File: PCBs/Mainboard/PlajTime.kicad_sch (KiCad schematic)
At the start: 7 parts, among them IC5 TXS0102DQMR, J10 2328702-4, J6 6pin_conn, J7 Phototransistor, J9 side button

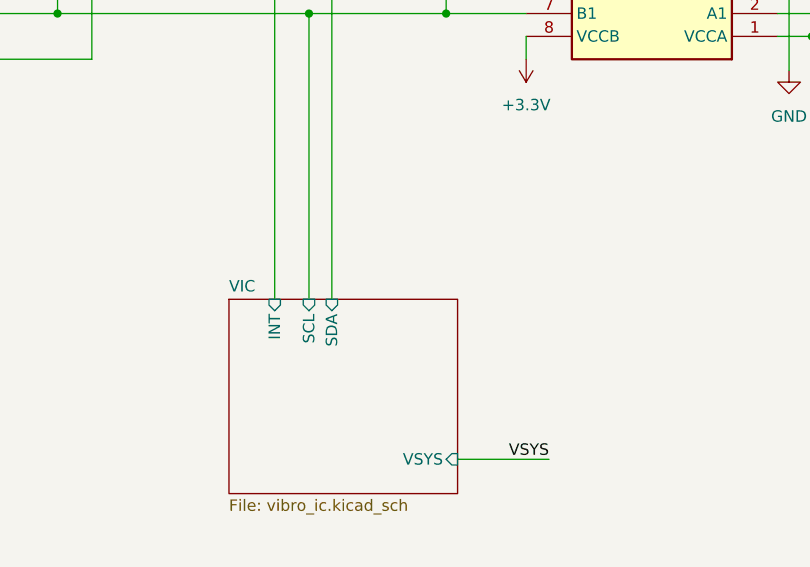
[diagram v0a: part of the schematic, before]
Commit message: added 3mf files to print
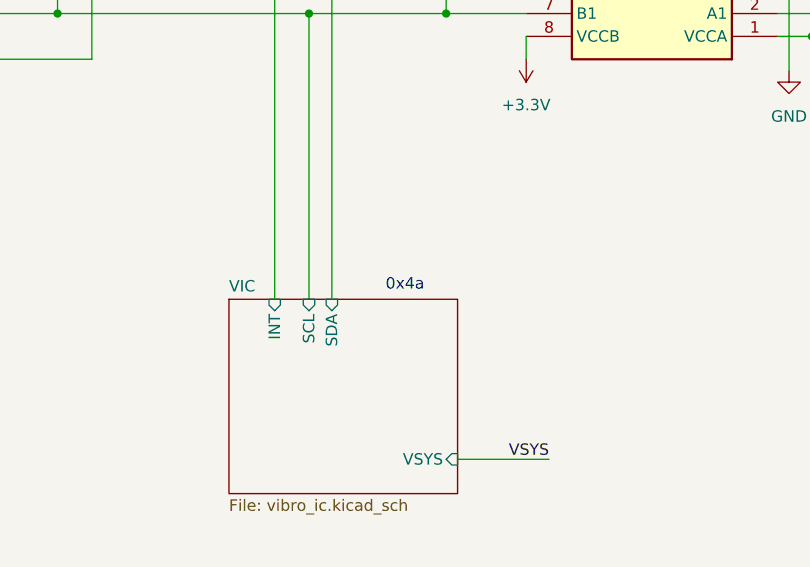
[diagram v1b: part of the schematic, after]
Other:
- note added: "0x4a"
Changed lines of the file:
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@@
+		)
+	)
+	(text "0x4a"
+		(exclude_from_sim no)
+		(at 198.628 133.096 0)
+		(effects
+			(font
+				(size 1.27 1.27)
+			)
 		)
 	)
